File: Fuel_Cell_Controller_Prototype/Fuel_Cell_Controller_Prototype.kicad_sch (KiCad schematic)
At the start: 43 parts, among them J3 6POS MOLEX, Q1 NMOS, Q2 NMOS, U3 MAX14572, U4 MAX14572, U6 SHT31-DIS, U7 BUF602xD, U8 BUF602xD

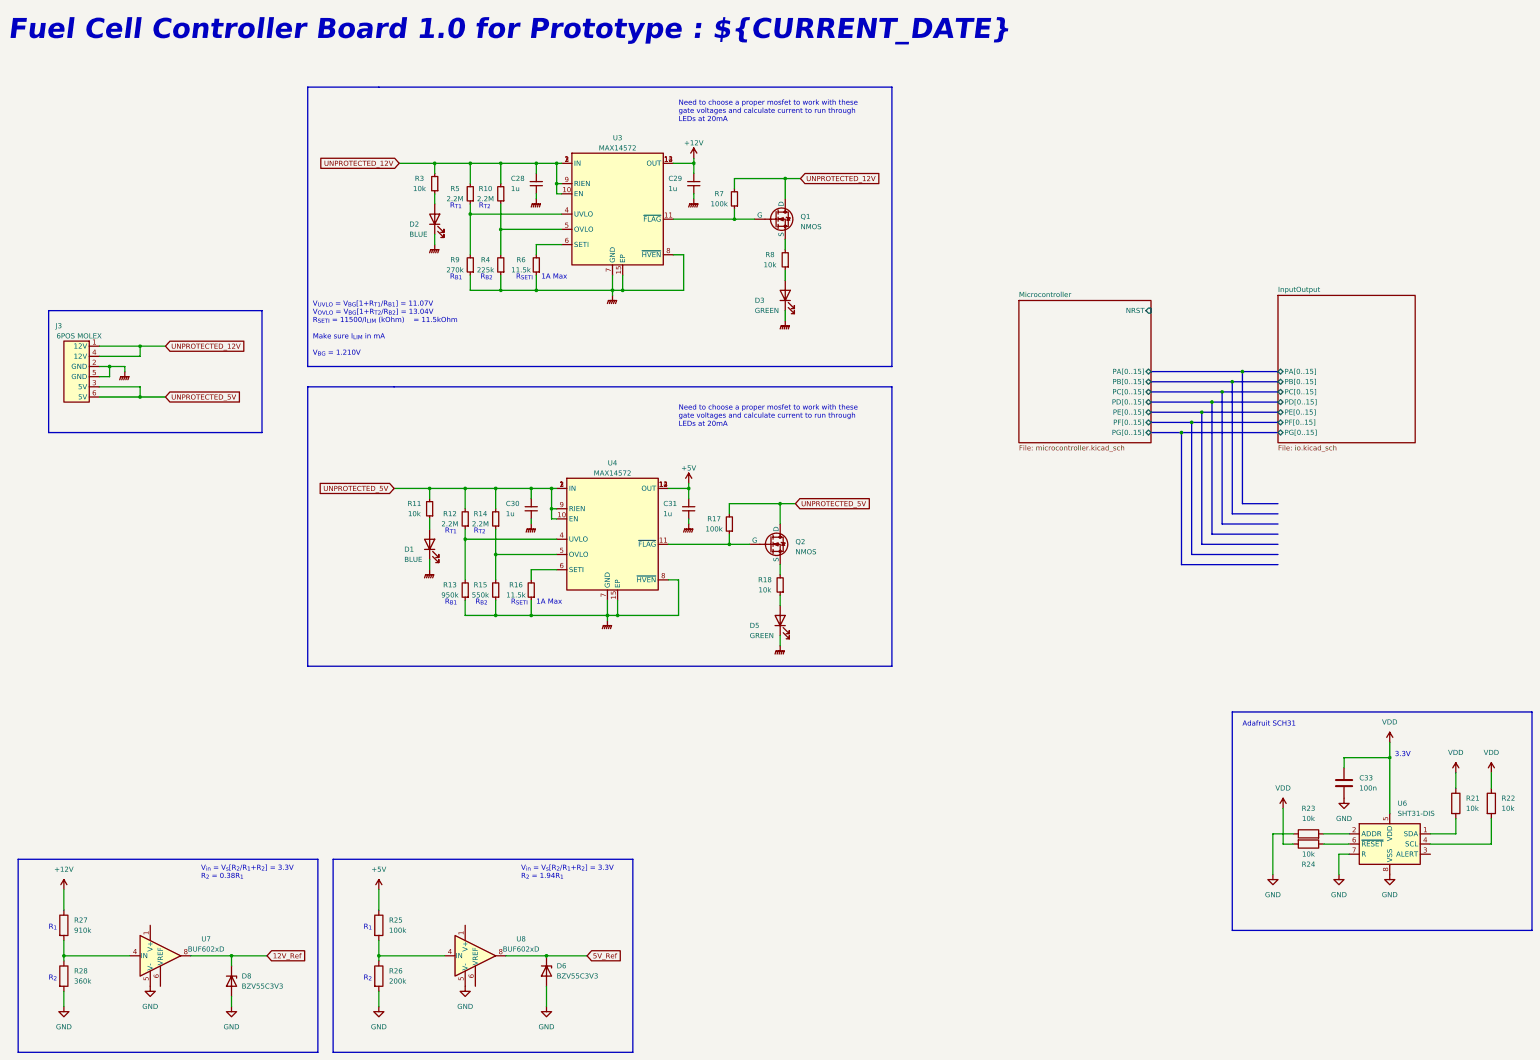
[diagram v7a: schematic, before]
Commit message: Added another 3.3V power supply to seperate from the MCU 3.3V ps
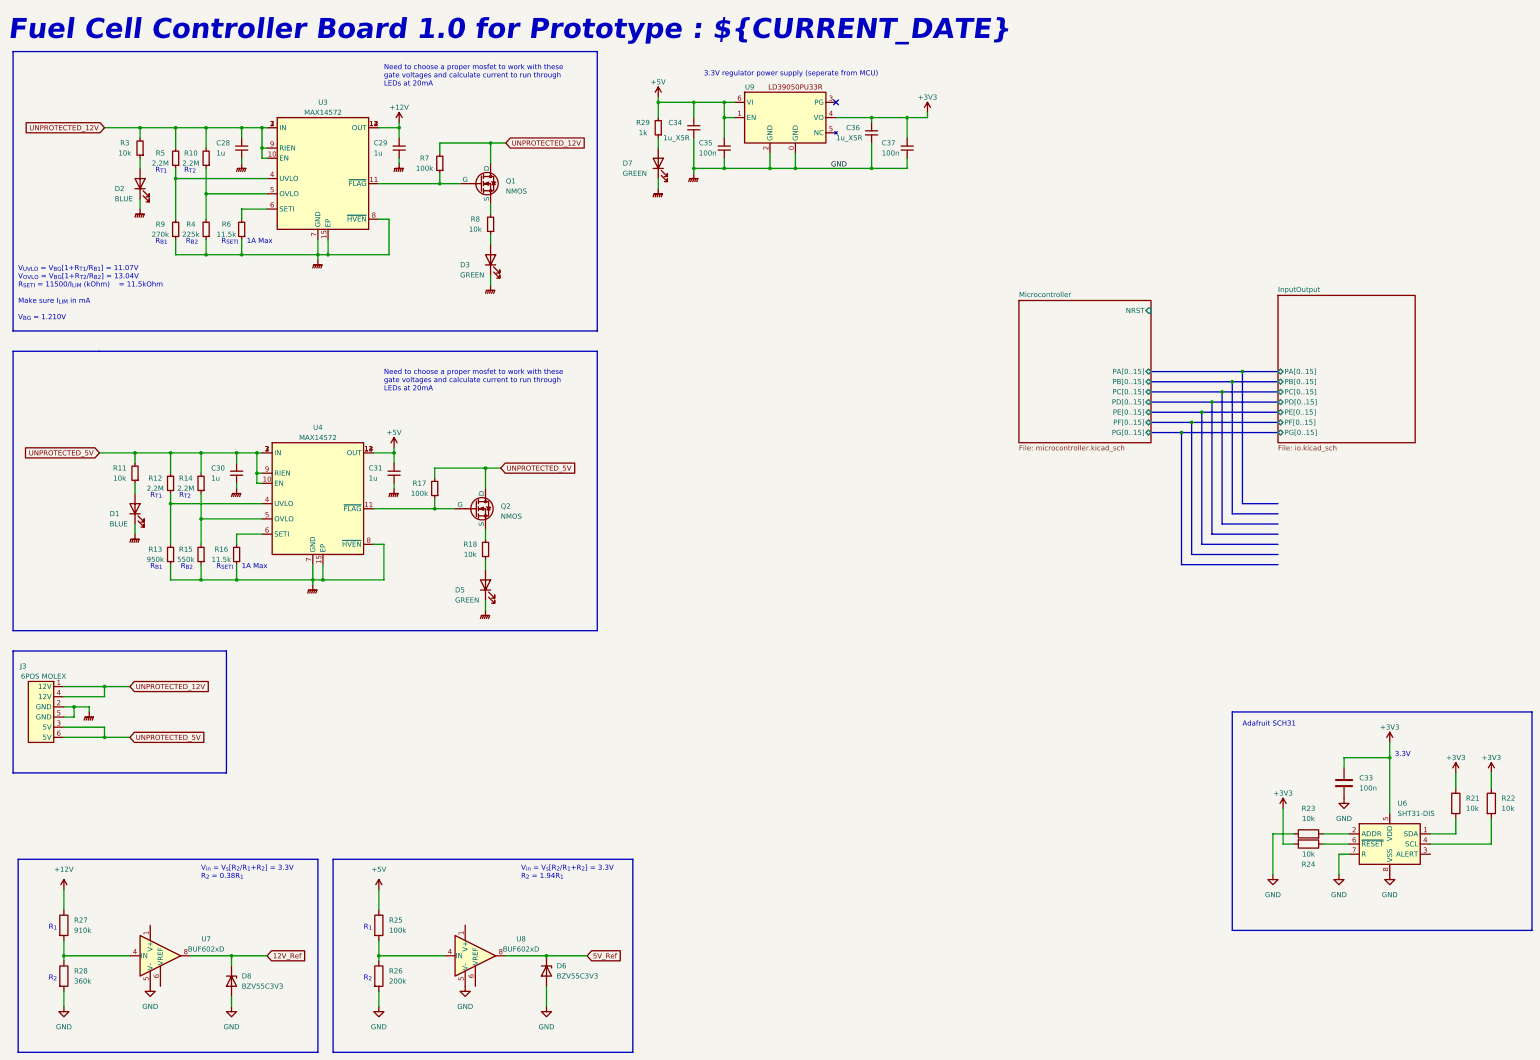
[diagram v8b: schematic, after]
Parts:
- added C34, C36: 1u_X5R, symbol Device:C_Small
- added C35, C37: 100n, symbol Device:C_Small
- added D7: GREEN, symbol Device:LED
- added R29: 1k, symbol Device:R_Small
- added U9: ~, symbol FCCParts:LD39050PU33R
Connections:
- net GNDPWR is gone; now on net GND: C28.1, C29.1, C30.1, C31.1, D1.1 (K), D2.1 (K), D3.1 (K), D5.1 (K), J3.2 (GND), J3.5 (GND), R13.1, R15.1, R16.1, R4.1, R6.1, R9.1, U3.15 (EP), U3.7 (GND), U3.8 (~{HVEN}), U4.15 (EP), U4.7 (GND), U4.8 (~{HVEN})
- net +5V: now also C34.2, C35.2, R29.2, U9.1 (EN), U9.6 (VI)
- net GND: now also C34.1, C35.1, C36.1, C37.1, D7.1 (K), U9.0 (GND), U9.2 (GND)
- net VDD renamed +3V3
- net +3V3: now also C36.2, C37.2, U9.4 (VO)
- new net: D7.2 (A), R29.1
- no-connect marks 0 -> 1
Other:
- note added: "3.3V regulator power supply (seperate from MCU)"
- moved on the sheet: C28, C29, C30, C31, D1, D2, D3, D5, J3, Q1, Q2, R10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
